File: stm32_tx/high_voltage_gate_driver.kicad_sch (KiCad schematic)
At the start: 9 parts, among them U15 IRS2186, U17 IRS2186, U18 ISO7760DW

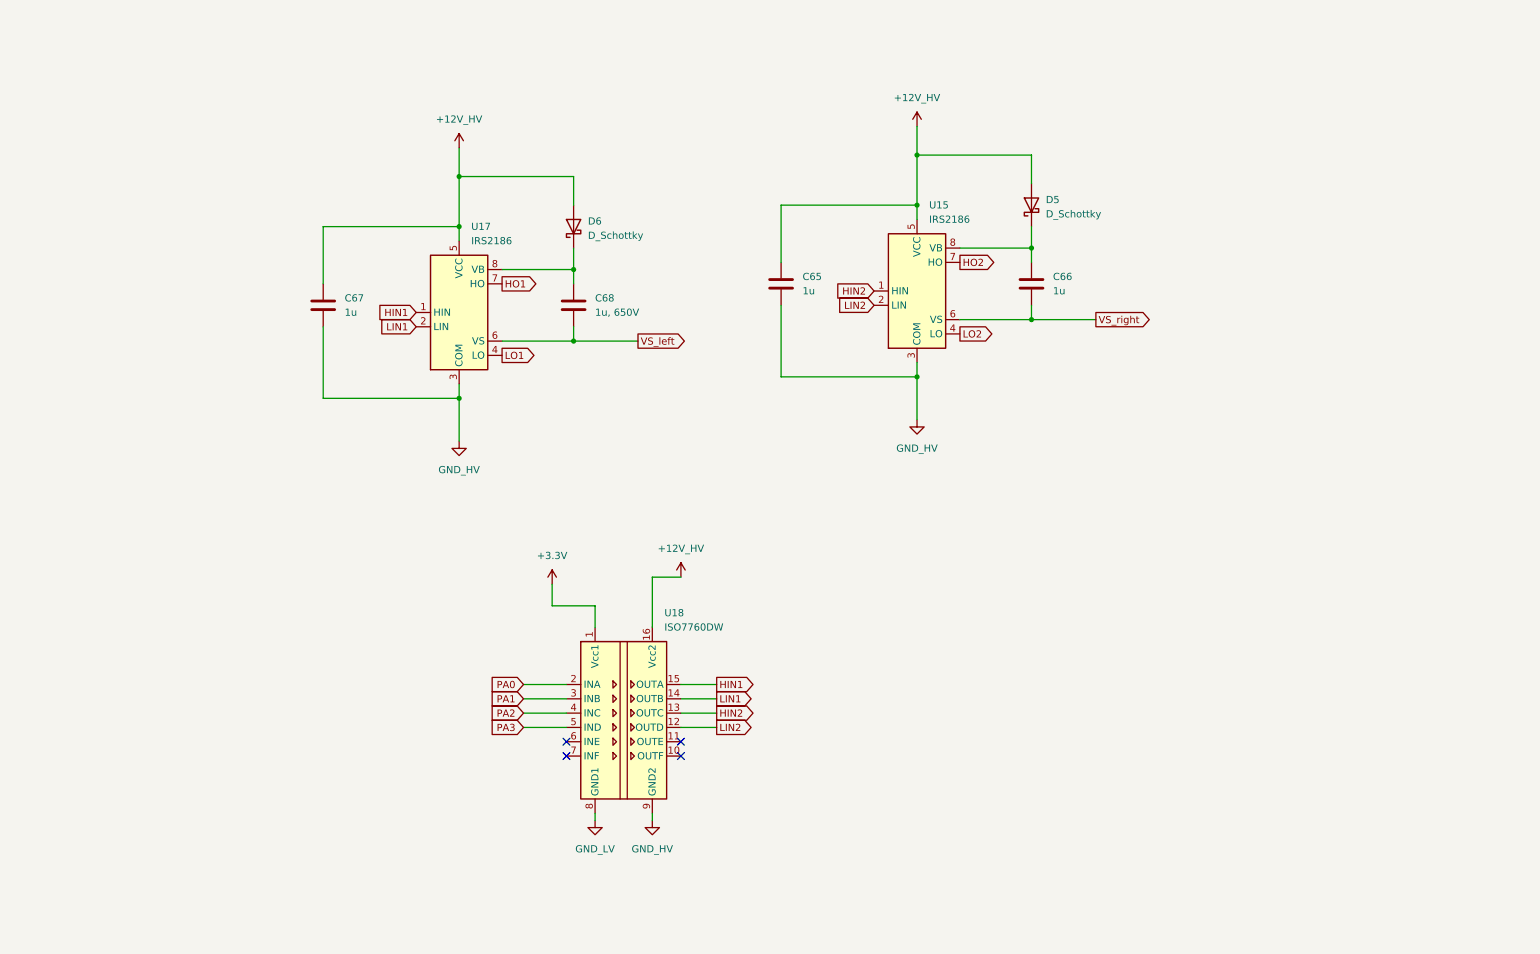
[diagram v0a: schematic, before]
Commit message: Added components and structure for analogue overvoltage and overcurrent protection
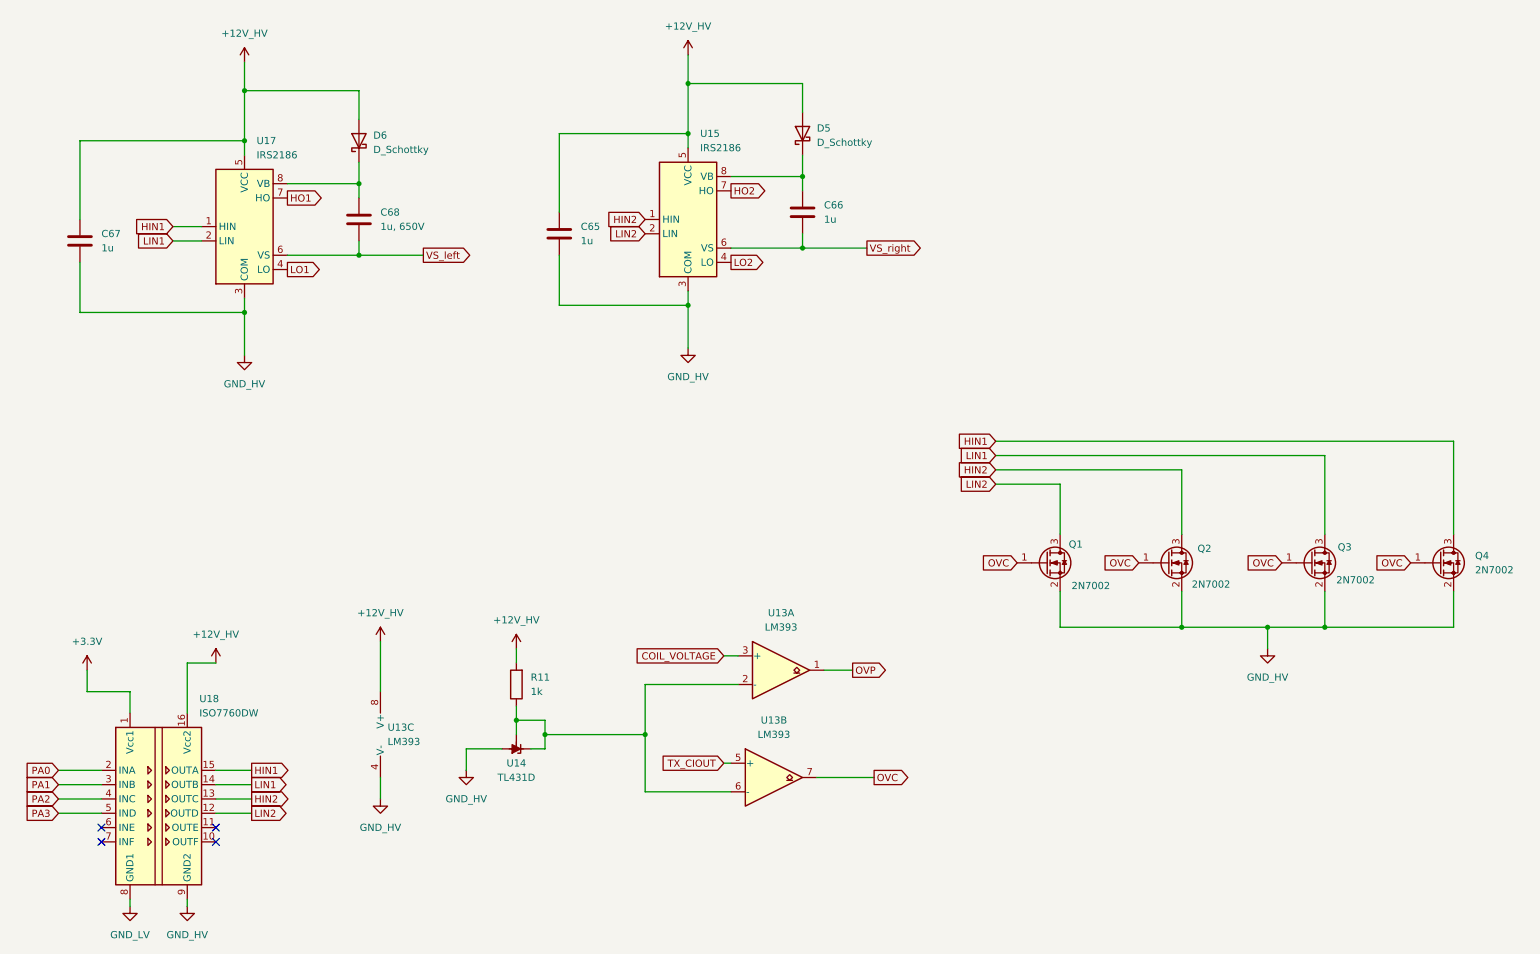
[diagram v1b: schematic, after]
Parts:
- added Q1, Q2, Q3, Q4: 2N7002, Package_TO_SOT_SMD:SOT-23, symbol Transistor_FET:2N7002
- added R11: 1k, symbol Device:R
- added U13: LM393, symbol Comparator:LM393
- added U14: TL431D, Package_SO:SOIC-8_3.9x4.9mm_P1.27mm, symbol Reference_Voltage:TL431D
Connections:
- net +12V_HV: now also R11.2, U13.8 (V+)
- net GND_HV: now also Q1.2 (S), Q2.2 (S), Q3.2 (S), Q4.2 (S), U13.4 (V-), U14.2 (A), U14.3 (A), U14.6 (A), U14.7 (A)
- net HIN1: now also Q4.3 (D)
- net HIN2: now also Q2.3 (D)
- net LIN1: now also Q3.3 (D)
- net LIN2: now also Q1.3 (D)
- new net: R11.1, U13.2 (-), U13.6 (-), U14.1 (K), U14.8 (REF)
- new net COIL_VOLTAGE: U13.3 (+)
- new net OVC: Q1.1 (G), Q2.1 (G), Q3.1 (G), Q4.1 (G), U13.7
- new net OVP: U13.1
- new net TX_CIOUT: U13.5 (+)
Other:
- moved on the sheet: C65, C66, C67, C68, D5, D6, U15, U17, U18

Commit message: Updated OVP and OVC to ahve seperate sources
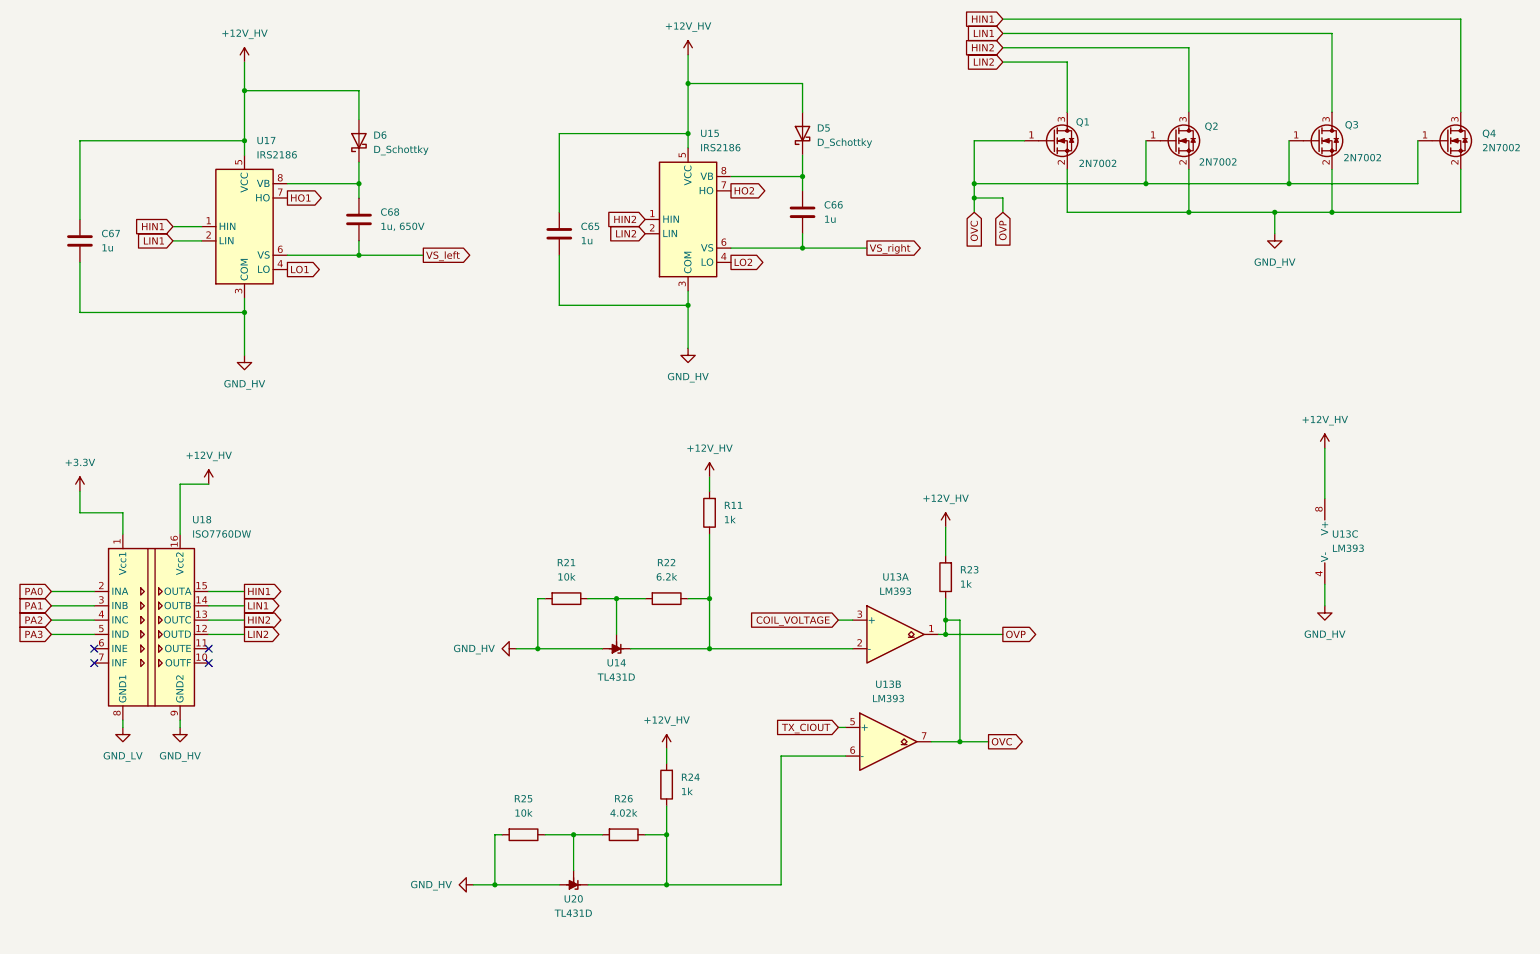
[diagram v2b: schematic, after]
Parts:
- added R21, R25: 10k, symbol Device:R
- added R22: 6.2k, symbol Device:R
- added R23, R24: 1k, symbol Device:R
- added R26: 4.02k, symbol Device:R
- added U20: TL431D, Package_SO:SOIC-8_3.9x4.9mm_P1.27mm, symbol Reference_Voltage:TL431D
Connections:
- net OVP is gone; now on net OVC: U13.1
- net +12V_HV: now also R23.2, R24.2
- net GND_HV: now also R21.2, R25.2, U20.2 (A), U20.3 (A), U20.6 (A), U20.7 (A)
- net OVC: now also R23.1
- net at R11.1, U13.2 (-), U14.1 (K): now also R22.1; no longer U13.6 (-), U14.8 (REF)
- new net: R21.1, R22.2, U14.8 (REF)
- new net: R24.1, R26.1, U13.6 (-), U20.1 (K)
- new net: R25.1, R26.2, U20.8 (REF)
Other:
- moved on the sheet: Q1, Q2, Q3, Q4, R11, U13A, U13B, U13C, U14, U18

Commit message: Added selected footprints
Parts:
- C65, C66, C67: footprint (none) -> Capacitor_SMD:C_0402_1005Metric
- R11: footprint (none) -> Resistor_SMD:R_0402_1005Metric
- R21, R22, R23, R24, R25, R26: footprint (none) -> Resistor_SMD:R_1206_3216Metric
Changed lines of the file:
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@@
 			)
 		)
-		(property "Footprint" ""
+		(property "Footprint" "Resistor_SMD:R_1206_3216Metric"
 			(at 114.3 121.412 90)
 			(effects
@@
 			)
 		)
-		(property "Footprint" ""
+		(property "Footprint" "Resistor_SMD:R_1206_3216Metric"
 			(at 124.46 163.322 90)
 			(effects
@@
 			)
 		)
-		(property "Footprint" ""
+		(property "Footprint" "Resistor_SMD:R_0402_1005Metric"
 			(at 141.478 107.95 90)
 			(effects
@@
 			)
 		)
-		(property "Footprint" ""
+		(property "Footprint" "Capacitor_SMD:C_0402_1005Metric"
 			(at 157.1752 58.42 0)
 			(effects
@@
 			)
 		)
-		(property "Footprint" ""
+		(property "Footprint" "Resistor_SMD:R_1206_3216Metric"
 			(at 133.858 156.21 90)
 			(effects
@@
 			)
 		)
-		(property "Footprint" ""
+		(property "Footprint" "Resistor_SMD:R_1206_3216Metric"
 			(at 132.08 121.412 90)
 			(effects
@@
 			)
 		)
-		(property "Footprint" ""
+		(property "Footprint" "Resistor_SMD:R_1206_3216Metric"
 			(at 183.388 119.38 90)
 			(effects
@@
 			)
 		)
-		(property "Footprint" ""
+		(property "Footprint" "Capacitor_SMD:C_0402_1005Metric"
 			(at 28.9052 63.5 0)
 			(effects
@@
 			)
 		)
-		(property "Footprint" ""
+		(property "Footprint" "Resistor_SMD:R_1206_3216Metric"
 			(at 106.68 163.322 90)
 			(effects
@@
 			)
 		)
-		(property "Footprint" ""
+		(property "Footprint" "Capacitor_SMD:C_0402_1005Metric"
 			(at 113.9952 62.23 0)
 			(effects
